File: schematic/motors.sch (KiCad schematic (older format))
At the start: 10 parts

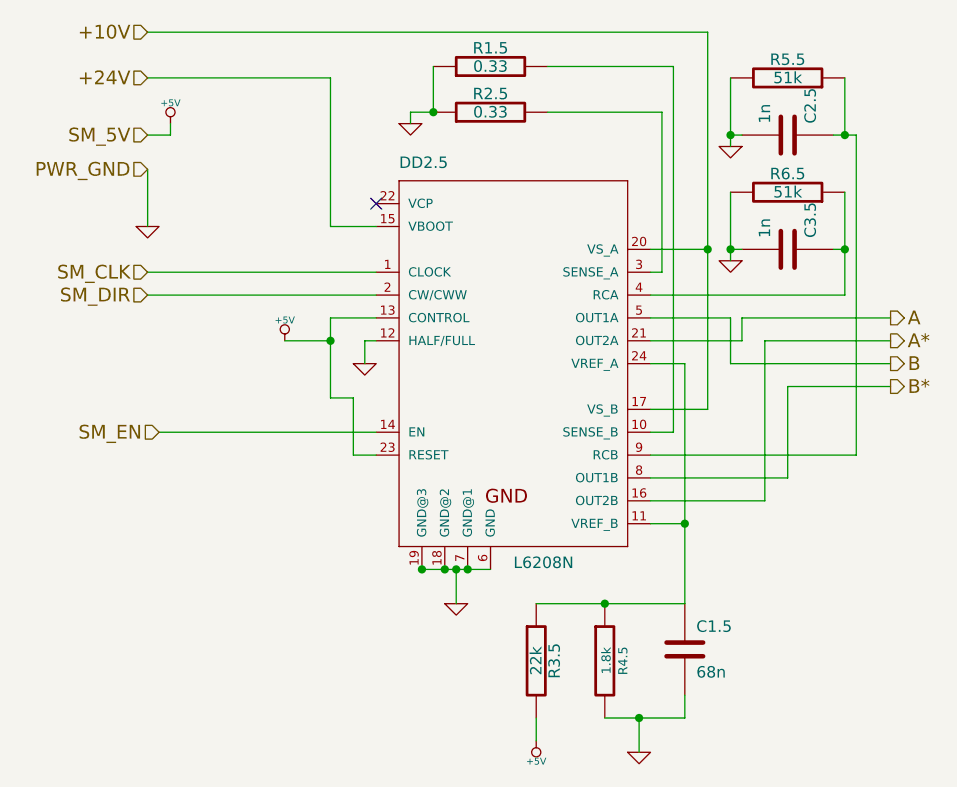
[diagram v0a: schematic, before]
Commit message: Shutter module tested
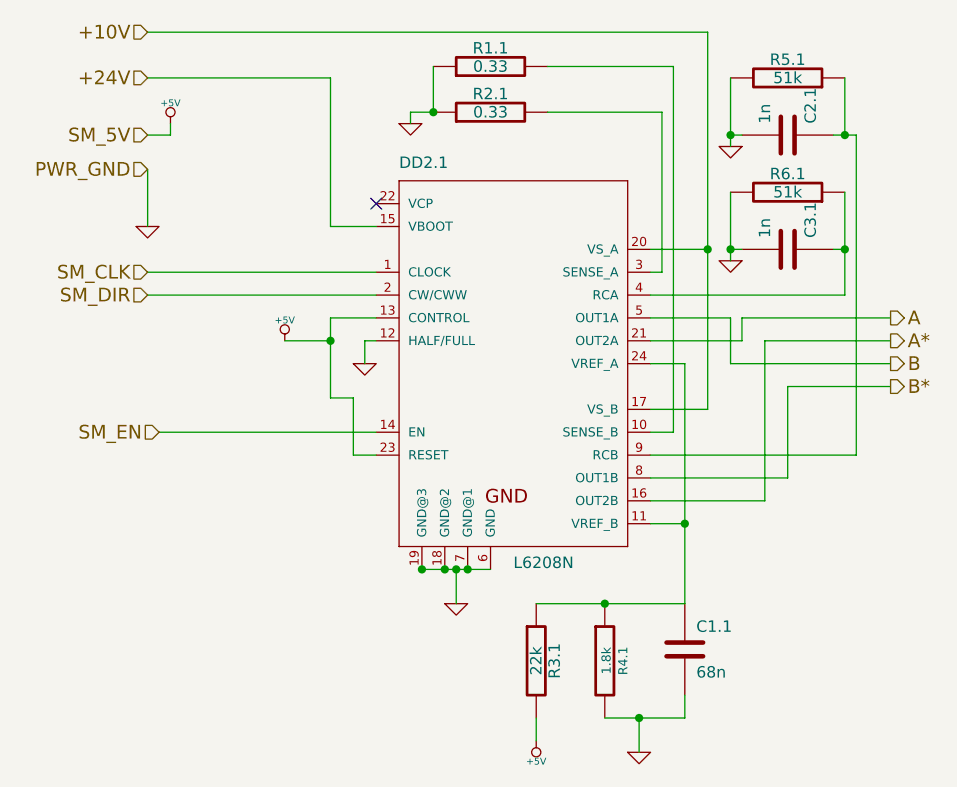
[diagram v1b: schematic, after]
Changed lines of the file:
@@
-EESchema Schematic File Version 2  date Ср 28 янв 2015 08:47:22
+EESchema Schematic File Version 2  date Ср 04 фев 2015 15:06:53
 LIBS:power
 LIBS:device
@@
 Sheet 8 12
 Title "Stepper motor module"
-Date "28 jan 2015"
+Date "4 feb 2015"
 Rev ""
 Comp "SAO RAS"
@@
 AR Path="/53A910BA/50CECA5D" Ref="C3.4"  Part="1"
 AR Path="/53A910B9/50CECA5D" Ref="C3.5"  Part="1"
-F 0 "C3.5" H 5550 3350 50  0000 L CNN
+F 0 "C3.1" H 5550 3350 50  0000 L CNN
 F 1 "1n" H 5550 3150 50  0000 L CNN
 F 2 "SM0805" H 5500 3250 60  0001 C CNN
@@
 AR Path="/53A910BA/50CECA5C" Ref="R6.4"  Part="1"
 AR Path="/53A910B9/50CECA5C" Ref="R6.5"  Part="1"
-F 0 "R6.5" V 5580 3000 50  0000 C CNN
+F 0 "R6.1" V 5580 3000 50  0000 C CNN
 F 1 "51k" V 5500 3000 50  0000 C CNN
 F 2 "SM0603" H 5500 3000 60  0001 C CNN
@@
 AR Path="/53A910BA/50CEC791" Ref="R5.4"  Part="1"
 AR Path="/53A910B9/50CEC791" Ref="R5.5"  Part="1"
-F 0 "R5.5" V 5580 2500 50  0000 C CNN
+F 0 "R5.1" V 5580 2500 50  0000 C CNN
 F 1 "51k" V 5500 2500 50  0000 C CNN
 F 2 "SM0603" H 5500 2500 60  0001 C CNN
@@
 AR Path="/53A910BA/50CEC790" Ref="C2.4"  Part="1"
 AR Path="/53A910B9/50CEC790" Ref="C2.5"  Part="1"
-F 0 "C2.5" H 5550 2850 50  0000 L CNN
+F 0 "C2.1" H 5550 2850 50  0000 L CNN
 F 1 "1n" H 5550 2650 50  0000 L CNN
 F 2 "SM0805" H 5500 2750 60  0001 C CNN
@@
 AR Path="/53A910BA/50CEB99A" Ref="R2.4"  Part="1"
 AR Path="/53A910B9/50CEB99A" Ref="R2.5"  Part="1"
-F 0 "R2.5" V 4280 2650 50  0000 C CNN
+F 0 "R2.1" V 4280 2650 50  0000 C CNN
 F 1 "0.33" V 4200 2650 50  0000 C CNN
 F 2 "SM2010" H 4200 2650 60  0001 C CNN
@@
 AR Path="/53A910BA/50CEB97A" Ref="R1.4"  Part="1"
 AR Path="/53A910B9/50CEB97A" Ref="R1.5"  Part="1"
-F 0 "R1.5" V 4280 2450 50  0000 C CNN
+F 0 "R1.1" V 4280 2450 50  0000 C CNN
 F 1 "0.33" V 4200 2450 50  0000 C CNN
 F 2 "SM2010" H 4200 2450 60  0001 C CNN
@@
 AR Path="/53A910BA/50AF1E60" Ref="C1.4"  Part="1"
 AR Path="/53A910B9/50AF1E60" Ref="C1.5"  Part="1"
-F 0 "C1.5" H 5100 5100 50  0000 L CNN
+F 0 "C1.1" H 5100 5100 50  0000 L CNN
 F 1 "68n" H 5100 4900 50  0000 L CNN
 F 2 "SM0805" H 5050 5000 60  0001 C CNN
@@
 AR Path="/53A910BA/50AF1C25" Ref="R3.4"  Part="1"
 AR Path="/53A910B9/50AF1C25" Ref="R3.5"  Part="1"
-F 0 "R3.5" V 4480 5050 50  0000 C CNN
+F 0 "R3.1" V 4480 5050 50  0000 C CNN
 F 1 "22k" V 4400 5050 50  0000 C CNN
 F 2 "SM0603" H 4400 5050 60  0001 C CNN
@@
 AR Path="/53A910BA/50AE2A4D" Ref="DD2.4"  Part="1"
 AR Path="/53A910B9/50AE2A4D" Ref="DD2.5"  Part="1"
-F 0 "DD2.5" H 3800 4600 50  0000 L BNN
+F 0 "DD2.1" H 3800 4600 50  0000 L BNN
 F 1 "L6208N" H 4300 2850 50  0000 L BNN
 F 2 "DIP-24__300_ELL" H 4300 3900 50  0001 C CNN
@@
 AR Path="/53A910BA/534BB108" Ref="R4.4"  Part="1"
 AR Path="/53A910B9/534BB108" Ref="R4.5"  Part="1"
-F 0 "R4.5" V 4780 5050 40  0000 C CNN
+F 0 "R4.1" V 4780 5050 40  0000 C CNN
 F 1 "1.8k" V 4707 5051 40  0000 C CNN
 F 2 "SM0603" V 4630 5050 30  0001 C CNN
